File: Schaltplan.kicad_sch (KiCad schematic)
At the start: 17 parts, among them K1 Relay, P1 USB Port vorheriger, P2 USB Port nächster, P4 USB Port Laden, U1 DC DC Wandler, U2 DC DC Wandler, U3 DS18B20, U4 Display, U5 DC DC Wandler, U6 Digitaler Poti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

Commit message: Add files via upload
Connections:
- net at P1.4 (D1): now also A1.11 (D8)
- net at P1.5 (D2): now also A1.13 (D10)
- net at K1. (NC): now also A1.7 (D4)
- net at P2.4 (D1): now also A1.12 (D9)
- net at P2.5 (D2): now also A1.14 (D11)
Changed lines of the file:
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@@
 		(color 0 0 0 0)
 	)
+	(bus_entry
+		(at 196.85 27.94)
+		(size 2.54 2.54)
+		(stroke
+			(width 0)
+			(type default)
+		)
+	)
+	(wire
+		(pts
+			(xy 172.72 128.27) (xy 189.23 128.27)
+		)
+		(stroke
+			(width 0)
+			(type default)
+		)
+	)
 	(wire
 		(pts
@@
 	(wire
 		(pts
+			(xy 53.34 17.78) (xy 173.99 17.78)
+		)
+		(stroke
+			(width 0)
+			(type default)
+		)
+	)
+	(wire
+		(pts
 			(xy 189.23 109.22) (xy 186.69 109.22)
 		)
@@
 	(wire
 		(pts
+			(xy 180.34 24.13) (xy 180.34 97.79)
+		)
+		(stroke
+			(width 0)
+			(type default)
+		)
+	)
+	(wire
+		(pts
 			(xy 170.18 63.5) (xy 170.18 191.77)
 		)
@@
 	(wire
 		(pts
+			(xy 52.07 72.39) (xy 52.07 16.51)
+		)
+		(stroke
+			(width 0)
+			(type default)
+		)
+	)
+	(wire
+		(pts
+			(xy 55.88 67.31) (xy 55.88 21.59)
+		)
+		(stroke
+			(width 0)
+			(type default)
+		)
+	)
+	(wire
+		(pts
 			(xy 99.06 181.61) (xy 115.57 181.61)
 		)
@@
 	(wire
 		(pts
+			(xy 58.42 64.77) (xy 58.42 24.13)
+		)
+		(stroke
+			(width 0)
+			(type default)
+		)
+	)
+	(wire
+		(pts
 			(xy 96.52 153.67) (xy 96.52 184.15)
 		)
@@
 	(wire
 		(pts
+			(xy 62.23 64.77) (xy 58.42 64.77)
+		)
+		(stroke
+			(width 0)
+			(type default)
+		)
+	)
+	(wire
+		(pts
+			(xy 171.45 16.51) (xy 172.72 128.27)
+		)
+		(stroke
+			(width 0)
+			(type default)
+		)
+	)
+	(wire
+		(pts
 			(xy 102.87 30.48) (xy 102.87 92.71)
 		)
@@
 	(wire
 		(pts
+			(xy 62.23 67.31) (xy 55.88 67.31)
+		)
+		(stroke
+			(width 0)
+			(type default)
+		)
+	)
+	(wire
+		(pts
 			(xy 104.14 147.32) (xy 109.22 147.32)
 		)
@@
 	(wire
 		(pts
+			(xy 62.23 69.85) (xy 53.34 69.85)
+		)
+		(stroke
+			(width 0)
+			(type default)
+		)
+	)
+	(wire
+		(pts
 			(xy 134.62 92.71) (xy 102.87 92.71)
 		)
@@
 	(wire
 		(pts
+			(xy 177.8 132.08) (xy 189.23 132.08)
+		)
+		(stroke
+			(width 0)
+			(type default)
+		)
+	)
+	(wire
+		(pts
+			(xy 173.99 17.78) (xy 173.99 93.98)
+		)
+		(stroke
+			(width 0)
+			(type default)
+		)
+	)
+	(wire
+		(pts
 			(xy 44.45 139.7) (xy 46.99 139.7)
 		)
@@
 	(wire
 		(pts
+			(xy 62.23 72.39) (xy 52.07 72.39)
+		)
+		(stroke
+			(width 0)
+			(type default)
+		)
+	)
+	(wire
+		(pts
+			(xy 55.88 21.59) (xy 177.8 21.59)
+		)
+		(stroke
+			(width 0)
+			(type default)
+		)
+	)
+	(wire
+		(pts
 			(xy 20.32 35.56) (xy 20.32 58.42)
 		)
@@
 	(wire
 		(pts
+			(xy 177.8 21.59) (xy 177.8 132.08)
+		)
+		(stroke
+			(width 0)
+			(type default)
+		)
+	)
+	(wire
+		(pts
 			(xy 74.93 95.25) (xy 57.15 95.25)
 		)
@@
 	(wire
 		(pts
+			(xy 58.42 24.13) (xy 180.34 24.13)
+		)
+		(stroke
+			(width 0)
+			(type default)
+		)
+	)
+	(wire
+		(pts
 			(xy 170.18 63.5) (xy 189.23 63.5)
 		)
@@
 	(wire
 		(pts
+			(xy 53.34 69.85) (xy 53.34 17.78)
+		)
+		(stroke
+			(width 0)
+			(type default)
+		)
+	)
+	(wire
+		(pts
 			(xy 157.48 177.8) (xy 146.05 177.8)
 		)
@@
 	(wire
 		(pts
+			(xy 180.34 97.79) (xy 189.23 97.79)
+		)
+		(stroke
+			(width 0)
+			(type default)
+		)
+	)
+	(wire
+		(pts
 			(xy 77.47 130.81) (xy 77.47 129.54)
 		)
@@
 	(wire
 		(pts
+			(xy 52.07 16.51) (xy 171.45 16.51)
+		)
+		(stroke
+			(width 0)
+			(type default)
+		)
+	)
+	(wire
+		(pts
 			(xy 44.45 187.96) (xy 63.5 187.96)
 		)
@@
 		)
 		(stroke
+			(width 0)
+			(type default)
+		)
+	)
+	(wire
+		(pts
+			(xy 173.99 93.98) (xy 189.23 93.98)
+		)
+		(stroke

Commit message: Cable moved
Co-authored-by: JumpStone <hi@jumpstone4477.de>
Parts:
- removed U3: DS18B20, Package_TO_SOT_THT:TO-92_Inline, symbol Sensor_Temperature:DS18B20
- removed U6: Digitaler Poti, Package_SO:MSOP-10_3x3mm_P0.5mm, symbol Potentiometer_Digital:DS3502
- added U3: Digitaler Poti, Package_SO:MSOP-10_3x3mm_P0.5mm, symbol Potentiometer_Digital:DS3502
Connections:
- net at A1.4 (GND), K1. (NC), U4.1 (GND)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: now also U3.2 (GND)
- net at A1.1 (D1/TX): now also U7.1 (CS)
- net at A1.27 (+5V), K1. (NC), U4.2 (VCC)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: now also U3.9 (V+)
- net at U7.1 (CS): now also A1.8 (D5)
- net at U7.10 (INC): now also A1.9 (D6)
- net at K1. (NC): now also A1.7 (D4)
- net at A1.25 (A6): now also U3.5 (A0)
- net at U1.6 (R1): now also U3.6 (RH)
- net at U1.7 (R2): now also U3.7 (RW)
- net at U1.8 (R3): now also U3.8 (RL)
- net at A1.10 (D7): now also U3.1 (CS)
- net at A1.15 (D12): now also U3.1 (CS)
- net at A1.16 (D13): now also U3.10 (INC)
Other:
- note removed: "Jeweils an den beiden Akkuzellen"

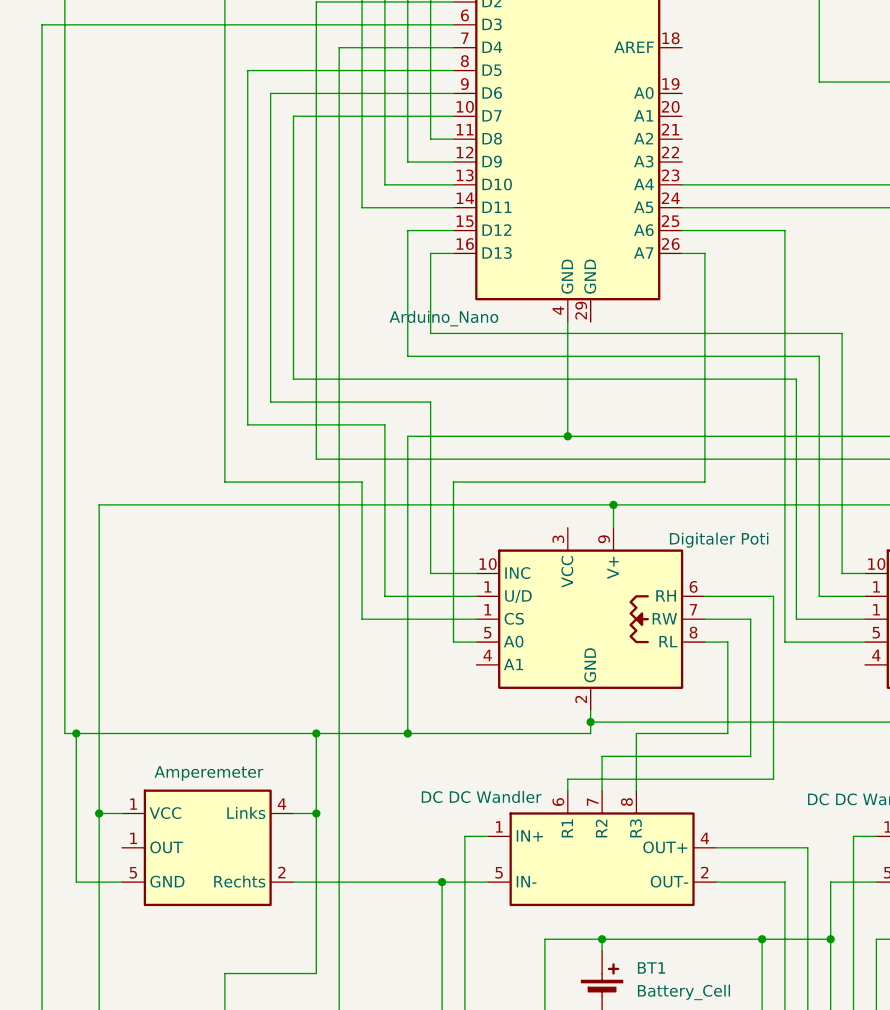
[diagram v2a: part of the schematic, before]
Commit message: Connected Ameperemeter
Co-authored-by: JumpStone <hi@jumpstone4477.de>
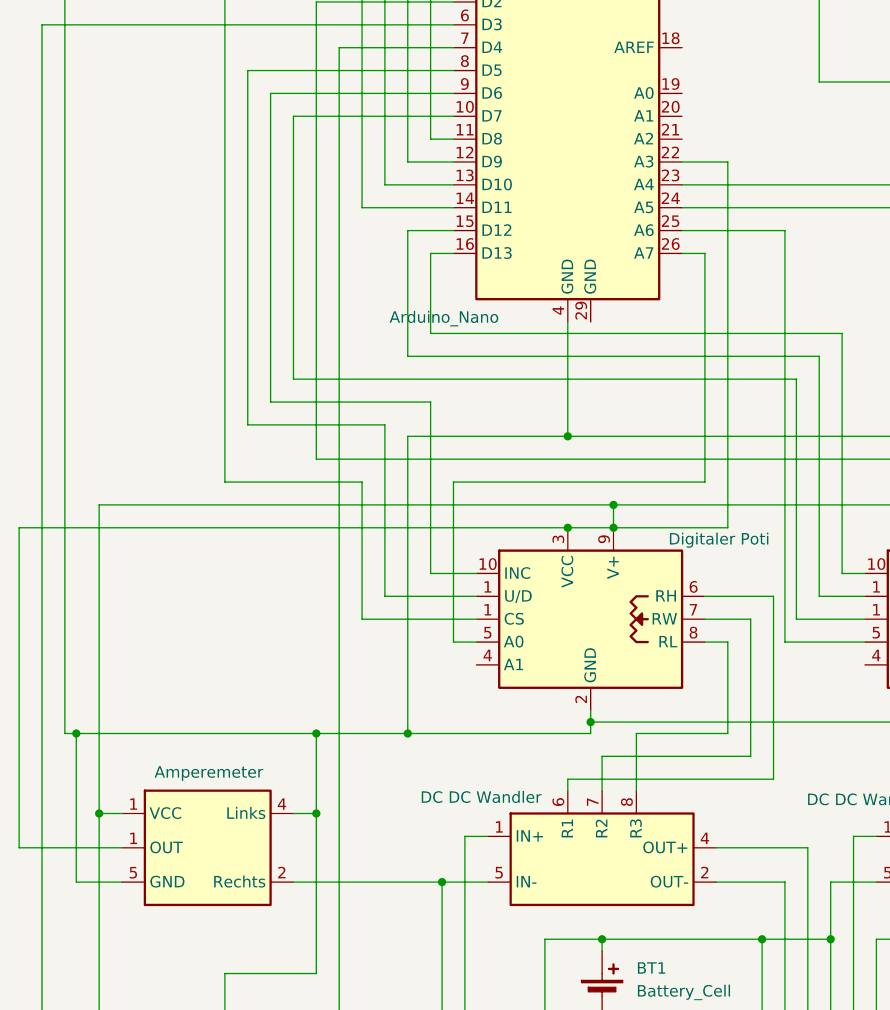
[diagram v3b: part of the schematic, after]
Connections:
- net at A1.27 (+5V), K1. (NC), U3.9 (V+)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: now also A1.22 (A3), U7.3 (VCC)
- net at K1. (NC): now also A1.7 (D4)
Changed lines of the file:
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@@
+	)
+	(junction
+		(at 74.93 107.95)
+		(diameter 0)
+		(color 0 0 0 0)
 	)
 	(junction
@@
 		(color 0 0 0 0)
 	)
+	(junction
+		(at 80.01 107.95)
+		(diameter 0)
+		(color 0 0 0 0)
+	)
 	(wire
 		(pts
@@
 	(wire
 		(pts
+			(xy 92.71 107.95) (xy 80.01 107.95)
+		)
+		(stroke
+			(width 0)
+			(type default)
+		)
+	)
+	(wire
+		(pts
 			(xy 62.23 64.77) (xy 59.69 64.77)
 		)
@@
 	(wire
 		(pts
+			(xy 87.63 67.31) (xy 92.71 67.31)
+		)
+		(stroke
+			(width 0)
+			(type default)
+		)
+	)
+	(wire
+		(pts
 			(xy 44.45 62.23) (xy 62.23 62.23)
 		)
@@
 	(wire
 		(pts
+			(xy 80.01 107.95) (xy 74.93 107.95)
+		)
+		(stroke
+			(width 0)
+			(type default)
+		)
+	)
+	(wire
+		(pts
 			(xy 77.47 129.54) (xy 120.65 129.54)
 		)
@@
 	(wire
 		(pts
+			(xy 92.71 67.31) (xy 92.71 107.95)
+		)
+		(stroke
+			(width 0)
+			(type default)
+		)
+	)
+	(wire
+		(pts
 			(xy 78.74 163.83) (xy 60.96 163.83)
 		)
@@
 	(wire
 		(pts
+			(xy 13.97 107.95) (xy 13.97 143.51)
+		)
+		(stroke
+			(width 0)
+			(type default)
+		)
+	)
+	(wire
+		(pts
 			(xy 46.99 157.48) (xy 46.99 139.7)
 		)
@@
 	(wire
 		(pts
+			(xy 13.97 143.51) (xy 25.4 143.51)
+		)
+		(stroke
+			(width 0)
+			(type default)
+		)
+	)
+	(wire
+		(pts
 			(xy 186.69 109.22) (xy 186.69 105.41)
 		)
 		(stroke
+			(width 0)
+			(type default)
+		)
+	)
+	(wire
+		(pts
+			(xy 74.93 107.95) (xy 13.97 107.95)
+		)
+		(stroke

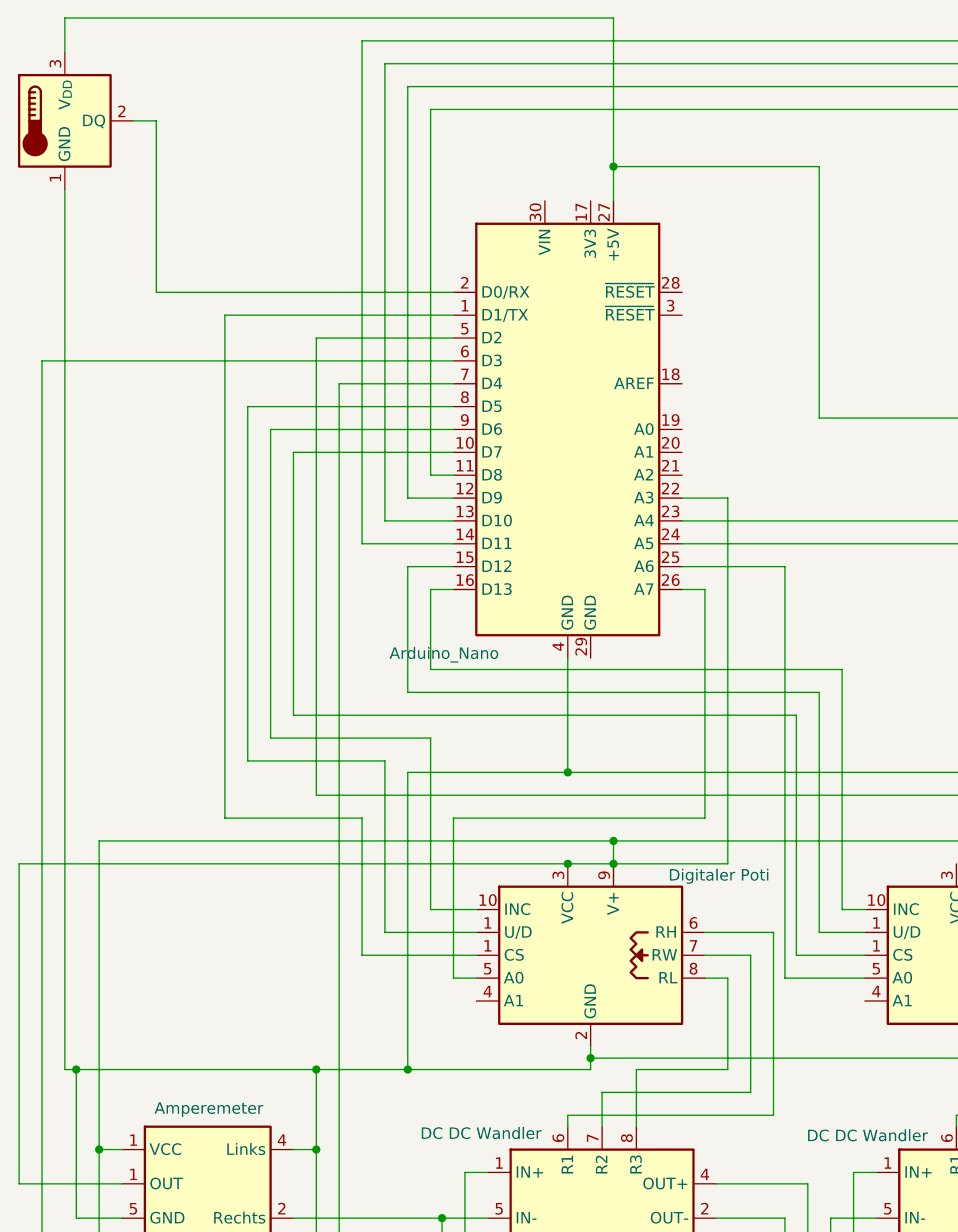
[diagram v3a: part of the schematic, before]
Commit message: Changed Pins Co-authored-by: JumpStone <hi@jumpstone4477.de>
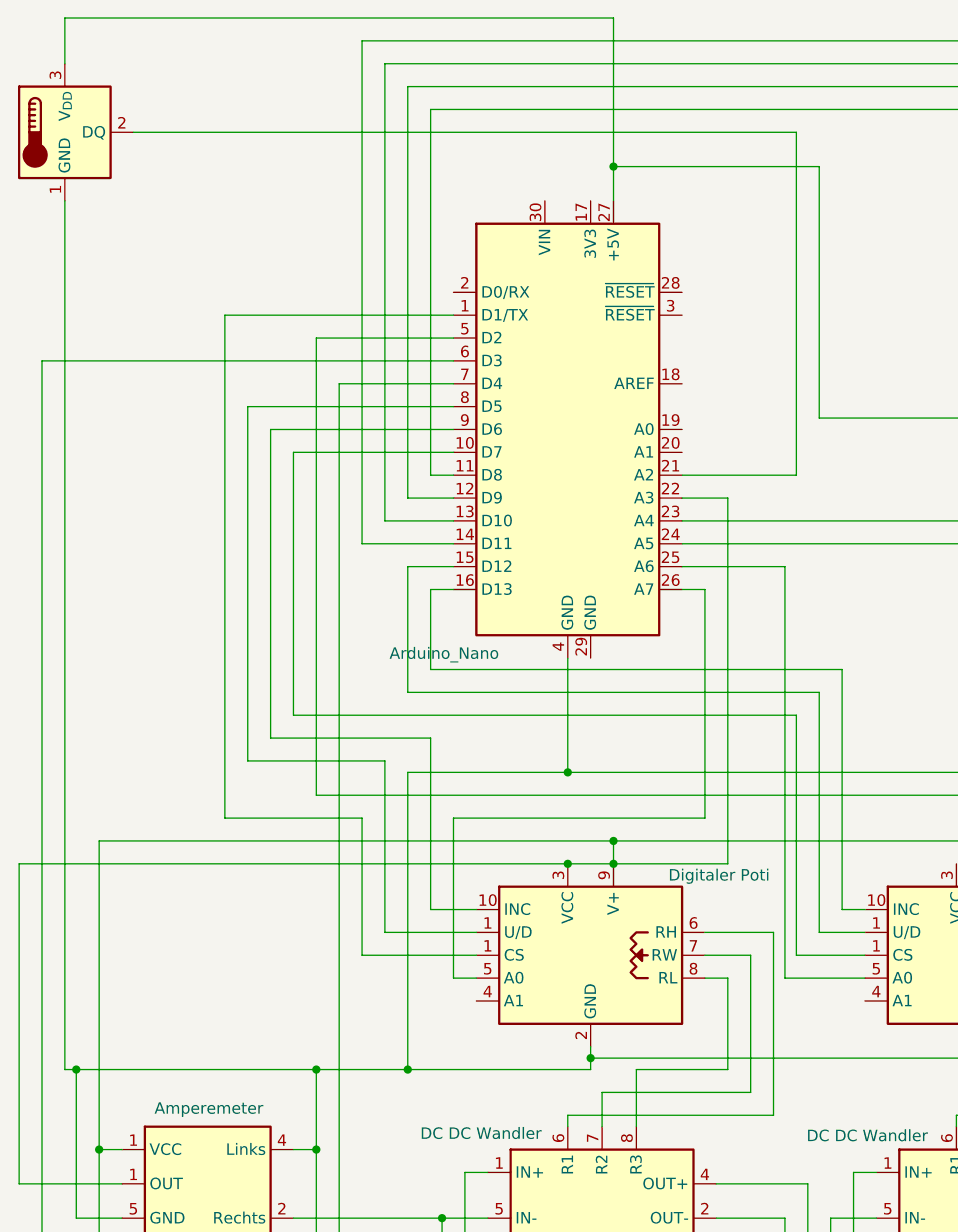
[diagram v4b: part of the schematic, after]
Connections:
- net at U9.2 (DQ): now also A1.21 (A2); no longer A1.2 (D0/RX)
- net at K1. (NC): now also A1.7 (D4)
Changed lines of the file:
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@@
-	(wire
-		(pts
-			(xy 26.67 25.4) (xy 29.21 25.4)
-		)
-		(stroke
-			(width 0)
-			(type default)
-		)
-	)
 	(wire
 		(pts
@@
 	(wire
 		(pts
+			(xy 26.67 26.67) (xy 100.33 26.67)
+		)
+		(stroke
+			(width 0)
+			(type default)
+		)
+	)
+	(wire
+		(pts
 			(xy 175.26 16.51) (xy 175.26 128.27)
 		)
@@
 	(wire
 		(pts
-			(xy 29.21 44.45) (xy 62.23 44.45)
-		)
-		(stroke
-			(width 0)
-			(type default)
-		)
-	)
-	(wire
-		(pts
 			(xy 121.92 133.35) (xy 138.43 133.35)
 		)
@@
 	(wire
 		(pts
-			(xy 19.05 33.02) (xy 19.05 130.81)
+			(xy 19.05 34.29) (xy 19.05 130.81)
 		)
 		(stroke
@@
 	(wire
 		(pts
-			(xy 19.05 13.97) (xy 19.05 17.78)
+			(xy 19.05 13.97) (xy 19.05 19.05)
 		)
 		(stroke
@@
 	(wire
 		(pts
-			(xy 29.21 25.4) (xy 29.21 44.45)
-		)
-		(stroke
-			(width 0)
-			(type default)
-		)
-	)
-	(wire
-		(pts
 			(xy 64.77 115.57) (xy 54.61 115.57)
 		)
@@
 	(wire
 		(pts
+			(xy 100.33 26.67) (xy 100.33 64.77)
+		)
+		(stroke
+			(width 0)
+			(type default)
+		)
+	)
+	(wire
+		(pts
 			(xy 80.01 105.41) (xy 123.19 105.41)
 		)
@@
 		(pts
 			(xy 74.93 97.79) (xy 57.15 97.79)
+		)
+		(stroke
+			(width 0)
+			(type default)
+		)
+	)
+	(wire
+		(pts
+			(xy 100.33 64.77) (xy 87.63 64.77)
 		)
 		(stroke
@@
 	(symbol
 		(lib_id "Sensor_Temperature:DS18B20")
-		(at 19.05 25.4 0)
+		(at 19.05 26.67 0)
 		(unit 1)
 		(exclude_from_sim no)
@@
 		(fields_autoplaced yes)
 		(property "Reference" "U9"
-			(at 12.7 24.1299 0)
+			(at 12.7 25.3999 0)
 			(effects
 				(font
@@
 		)
 		(property "Value" "DS18B20"
-			(at 12.7 26.6699 0)
+			(at 12.7 27.9399 0)
 			(effects
 				(font
@@
 		)
 		(property "Footprint" "Package_TO_SOT_THT:TO-92_Inline"
-			(at -6.35 31.75 0)
+			(at -6.35 33.02 0)
 			(effects
 				(font
@@
 		)
 		(property "Datasheet" "http://datasheets.maximintegrated.com/en/ds/DS18B20.pdf"
-			(at 15.24 19.05 0)
+			(at 15.24 20.32 0)
 			(effects
 				(font
@@
 		)
 		(property "Description" "Programmable Resolution 1-Wire Digital Thermometer TO-92"
-			(at 19.05 25.4 0)
-			(effects
-				(font
+			(at 19.05 26.67 0)
+			(effects
+				(font
